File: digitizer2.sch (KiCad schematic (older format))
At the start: 4 parts, among them U1 XC7A35T, U2 FT2232H, U3 MT41J128M16, U4 ADS5403

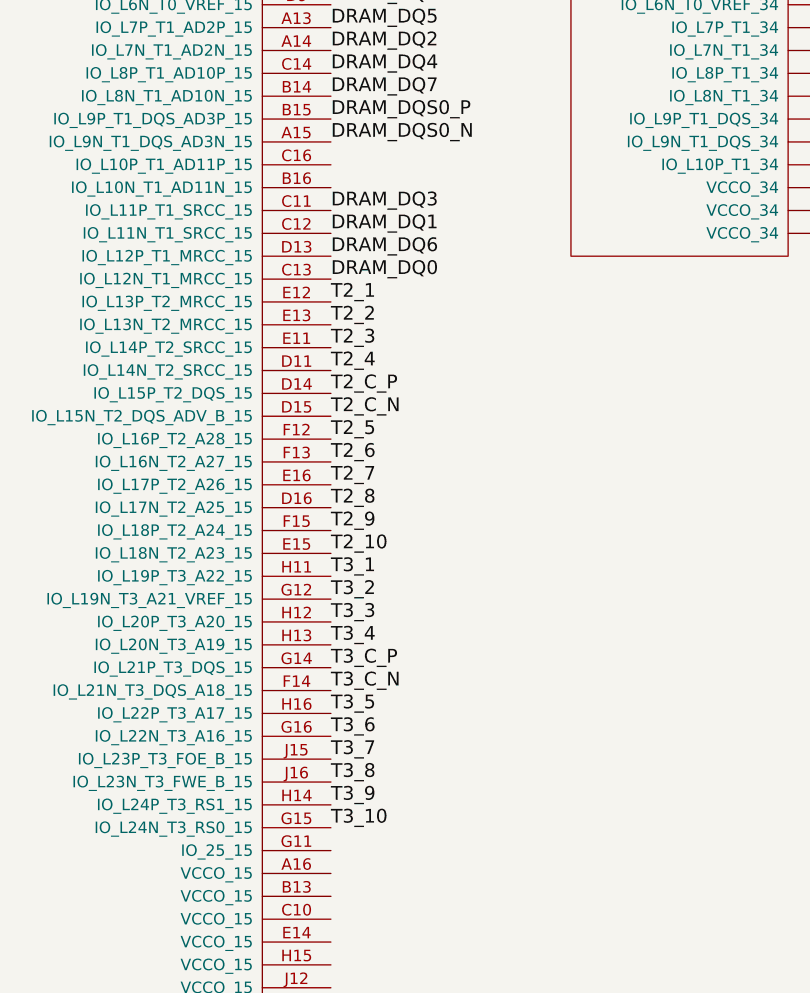
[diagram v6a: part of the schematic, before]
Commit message: Begin DDR Addr/Ctrl tuning
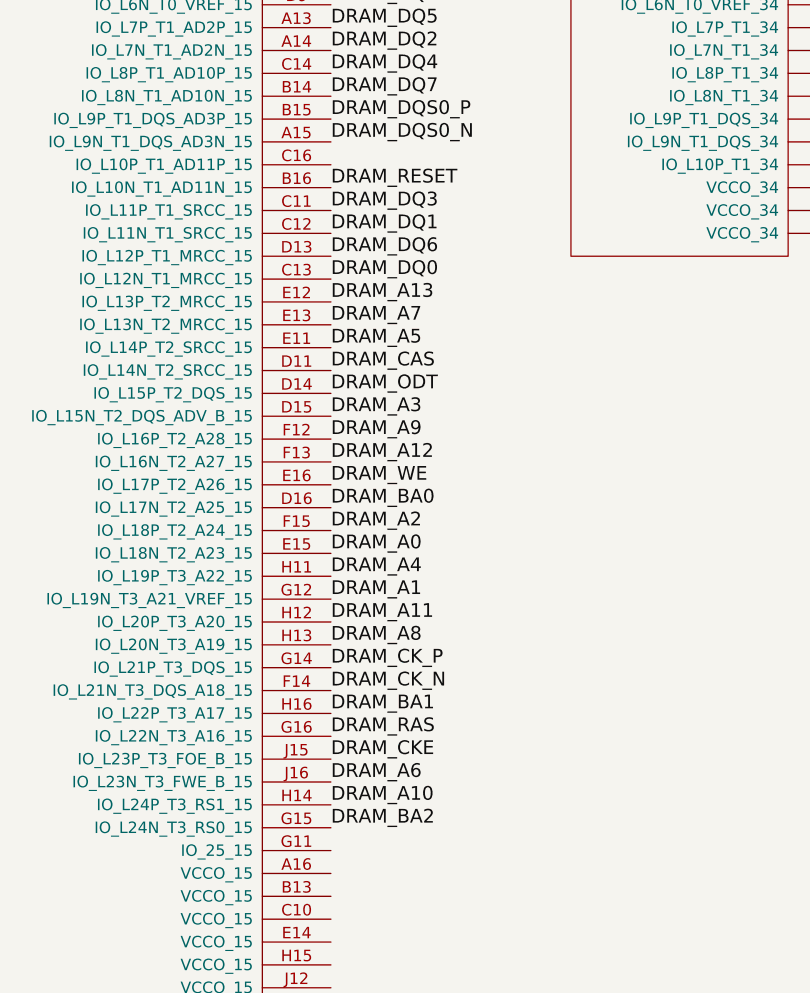
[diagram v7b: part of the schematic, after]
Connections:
- net T2_1 is gone; now on net DRAM_A13: U1.E12 (IO_L13P_T2_MRCC_15)
- net T2_10 is gone; now on net DRAM_A0: U1.E15 (IO_L18N_T2_A23_15)
- net T2_2 is gone; now on net DRAM_A7: U1.E13 (IO_L13N_T2_MRCC_15)
- net T2_3 is gone; now on net DRAM_A5: U1.E11 (IO_L14P_T2_SRCC_15)
- net T2_4 is gone; now on net DRAM_CAS: U1.D11 (IO_L14N_T2_SRCC_15)
- net T2_5 is gone; now on net DRAM_A9: U1.F12 (IO_L16P_T2_A28_15)
- net T2_6 is gone; now on net DRAM_A12: U1.F13 (IO_L16N_T2_A27_15)
- net T2_7 is gone; now on net DRAM_WE: U1.E16 (IO_L17P_T2_A26_15)
- net T2_8 is gone; now on net DRAM_BA0: U1.D16 (IO_L17N_T2_A25_15)
- net T2_9 is gone; now on net DRAM_A2: U1.F15 (IO_L18P_T2_A24_15)
- net T2_C_N is gone; now on net DRAM_A3: U1.D15 (IO_L15N_T2_DQS_ADV_B_15)
- net T2_C_P is gone; now on net DRAM_ODT: U1.D14 (IO_L15P_T2_DQS_15)
- net T3_1 is gone; now on net DRAM_A4: U1.H11 (IO_L19P_T3_A22_15)
- net T3_10 is gone; now on net DRAM_BA2: U1.G15 (IO_L24N_T3_RS0_15)
- net T3_2 is gone; now on net DRAM_A1: U1.G12 (IO_L19N_T3_A21_VREF_15)
- net T3_3 is gone; now on net DRAM_A11: U1.H12 (IO_L20P_T3_A20_15)
- net T3_4 is gone; now on net DRAM_A8: U1.H13 (IO_L20N_T3_A19_15)
- net T3_5 is gone; now on net DRAM_BA1: U1.H16 (IO_L22P_T3_A17_15)
- net T3_6 is gone; now on net DRAM_RAS: U1.G16 (IO_L22N_T3_A16_15)
- net T3_7 is gone; now on net DRAM_CKE: U1.J15 (IO_L23P_T3_FOE_B_15)
- net T3_8 is gone; now on net DRAM_A6: U1.J16 (IO_L23N_T3_FWE_B_15)
- net T3_9 is gone; now on net DRAM_A10: U1.H14 (IO_L24P_T3_RS1_15)
- net T3_C_N is gone; now on net DRAM_CK_N: U1.F14 (IO_L21N_T3_DQS_A18_15)
- net T3_C_P is gone; now on net DRAM_CK_P: U1.G14 (IO_L21P_T3_DQS_15)
- net DRAM_RESET: now also U1.B16 (IO_L10N_T1_AD11N_15)
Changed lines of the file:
@@
 DRAM_DQ0
 Text Label 6950 3400 0    60   ~ 0
-T2_1
+DRAM_A13
 Text Label 6950 3500 0    60   ~ 0
-T2_2
+DRAM_A7
 Text Label 6950 3600 0    60   ~ 0
-T2_3
+DRAM_A5
 Text Label 6950 3700 0    60   ~ 0
-T2_4
+DRAM_CAS
 Text Label 6950 4000 0    60   ~ 0
-T2_5
+DRAM_A9
 Text Label 6950 4100 0    60   ~ 0
-T2_6
+DRAM_A12
 Text Label 6950 4200 0    60   ~ 0
-T2_7
+DRAM_WE
 Text Label 6950 4300 0    60   ~ 0
-T2_8
+DRAM_BA0
 Text Label 6950 4400 0    60   ~ 0
-T2_9
+DRAM_A2
 Text Label 6950 4500 0    60   ~ 0
-T2_10
+DRAM_A0
 Text Label 6950 3800 0    60   ~ 0
-T2_C_P
+DRAM_ODT
 Text Label 6950 3900 0    60   ~ 0
-T2_C_N
+DRAM_A3
 Text Label 6950 2600 0    60   ~ 0
 DRAM_DQS0_P
@@
 DRAM_DQS0_N
 Text Label 6950 4600 0    60   ~ 0
-T3_1
+DRAM_A4
 Text Label 6950 4700 0    60   ~ 0
-T3_2
+DRAM_A1
 Text Label 6950 4800 0    60   ~ 0
-T3_3
+DRAM_A11
 Text Label 6950 4900 0    60   ~ 0
-T3_4
+DRAM_A8
 Text Label 6950 5000 0    60   ~ 0
-T3_C_P
+DRAM_CK_P
 Text Label 6950 5100 0    60   ~ 0
-T3_C_N
+DRAM_CK_N
 Text Label 6950 5200 0    60   ~ 0
-T3_5
+DRAM_BA1
 Text Label 6950 5300 0    60   ~ 0
-T3_6
+DRAM_RAS
 Text Label 6950 5400 0    60   ~ 0
-T3_7
+DRAM_CKE
 Text Label 6950 5500 0    60   ~ 0
-T3_8
+DRAM_A6
 Text Label 6950 5600 0    60   ~ 0
-T3_9
+DRAM_A10
 Text Label 6950 5700 0    60   ~ 0
-T3_10
+DRAM_BA2
+Text Label 6950 2900 0    60   ~ 0
+DRAM_RESET
 $EndSCHEMATC

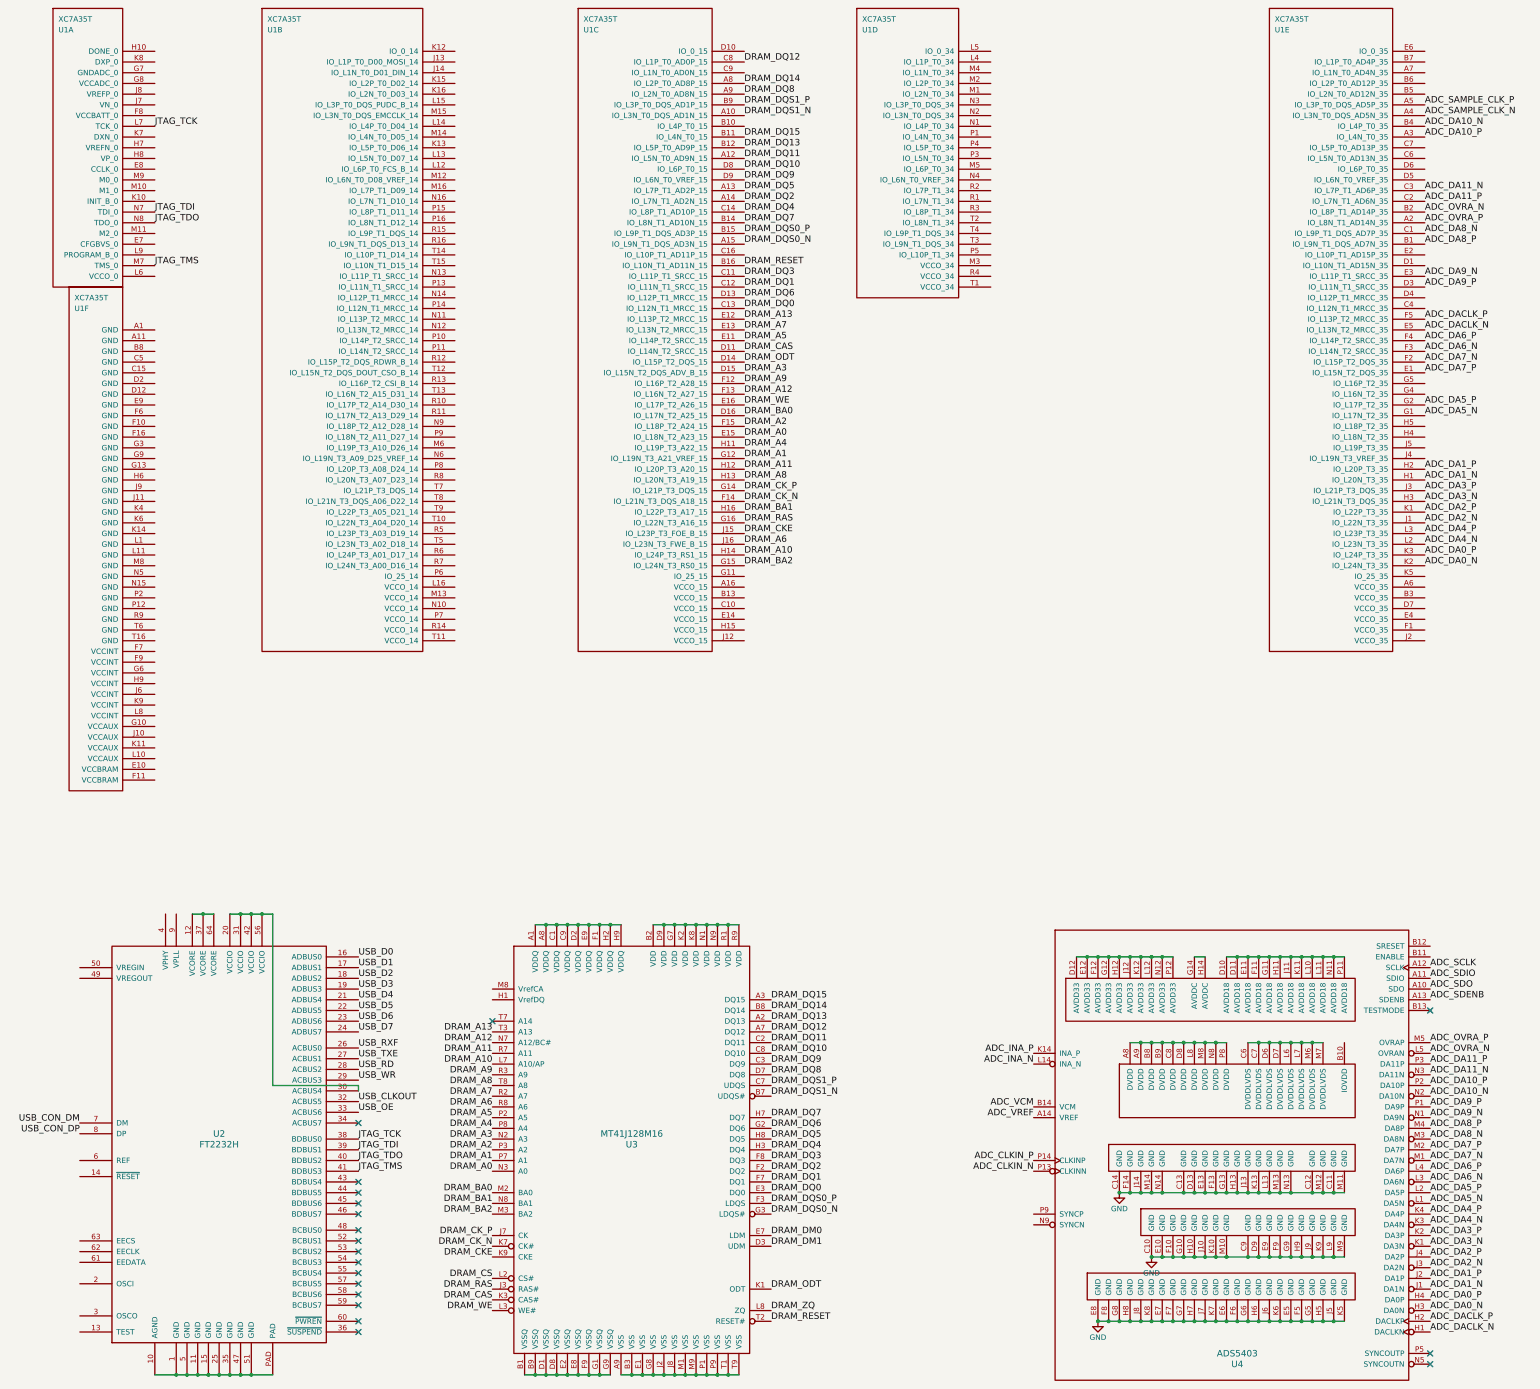
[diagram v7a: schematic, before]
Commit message: Layout FTDI interface
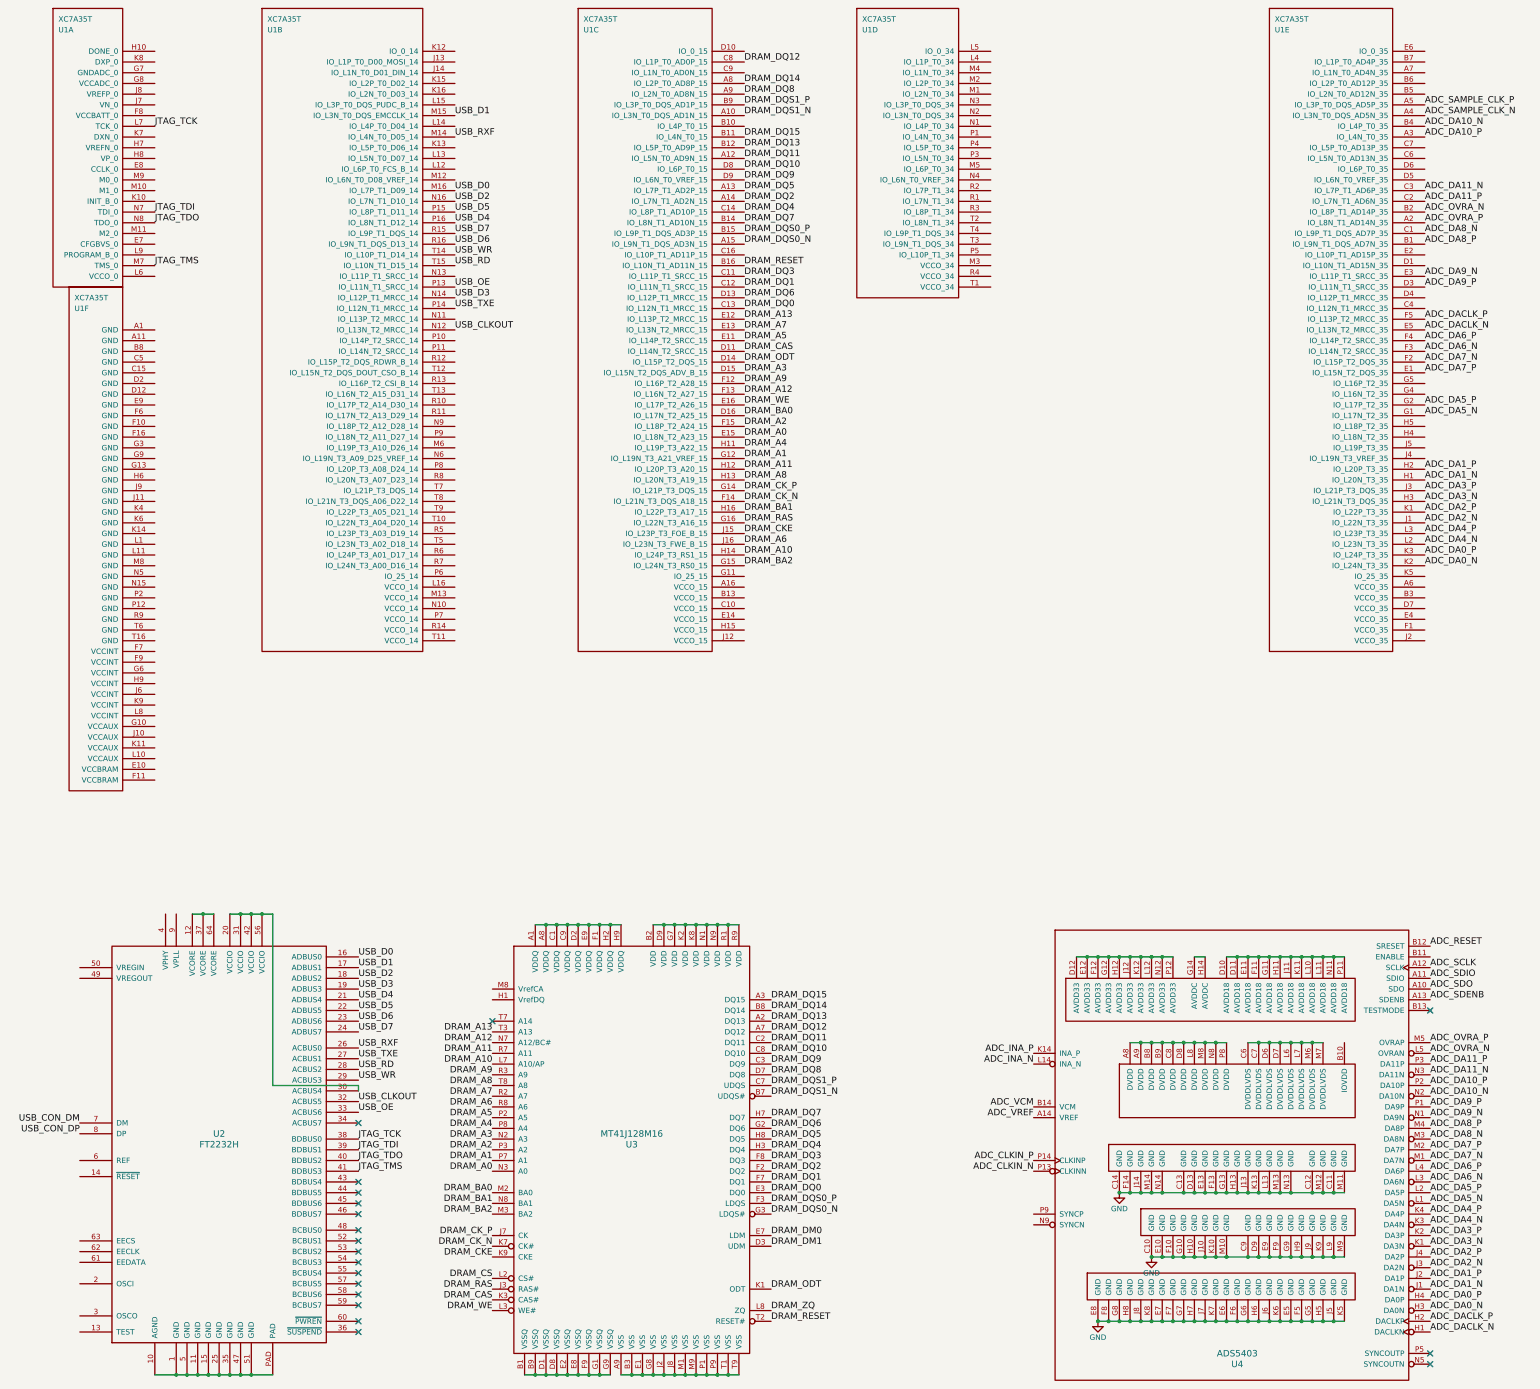
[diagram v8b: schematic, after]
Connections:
- net USB_CLKOUT: now also U1.N12 (IO_L13N_T2_MRCC_14)
- net USB_D0: now also U1.M16 (IO_L7P_T1_D09_14)
- net USB_D1: now also U1.M15 (IO_L3N_T0_DQS_EMCCLK_14)
- net USB_D2: now also U1.N16 (IO_L7N_T1_D10_14)
- net USB_D3: now also U1.N14 (IO_L12P_T1_MRCC_14)
- net USB_D4: now also U1.P16 (IO_L8N_T1_D12_14)
- net USB_D5: now also U1.P15 (IO_L8P_T1_D11_14)
- net USB_D6: now also U1.R16 (IO_L9N_T1_DQS_D13_14)
- net USB_D7: now also U1.R15 (IO_L9P_T1_DQS_14)
- net USB_OE: now also U1.P13 (IO_L11N_T1_SRCC_14)
- net USB_RD: now also U1.T15 (IO_L10N_T1_D15_14)
- net USB_RXF: now also U1.M14 (IO_L4N_T0_D05_14)
- net USB_TXE: now also U1.P14 (IO_L12N_T1_MRCC_14)
- net USB_WR: now also U1.T14 (IO_L10P_T1_D14_14)
- net ADC_RESET: now reaches U4.B12 (SRESET)
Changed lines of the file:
@@
 Text Label 6950 2900 0    60   ~ 0
 DRAM_RESET
+Text Label 4250 2200 0    60   ~ 0
+USB_D0
+Text Label 4250 1500 0    60   ~ 0
+USB_D1
+Text Label 4250 2300 0    60   ~ 0
+USB_D2
+Text Label 4250 3200 0    60   ~ 0
+USB_D3
+Text Label 4250 2500 0    60   ~ 0
+USB_D4
+Text Label 4250 2400 0    60   ~ 0
+USB_D5
+Text Label 4250 2700 0    60   ~ 0
+USB_D6
+Text Label 4250 2600 0    60   ~ 0
+USB_D7
+Text Label 4250 1700 0    60   ~ 0
+USB_RXF
+Text Label 4250 3300 0    60   ~ 0
+USB_TXE
+Text Label 4250 2900 0    60   ~ 0
+USB_RD
+Text Label 4250 2800 0    60   ~ 0
+USB_WR
+Text Label 4250 3100 0    60   ~ 0
+USB_OE
+Text Label 4250 3500 0    60   ~ 0
+USB_CLKOUT
+Text Label 13350 9250 0    60   ~ 0
+ADC_RESET
 $EndSCHEMATC
